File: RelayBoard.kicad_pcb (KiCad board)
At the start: 4 copper layers, 211.1 x 95.2 mm, 103 parts, among them J1 CONN_03-SCREW-5MM, J10 AC In, J11 CONN_03-SCREW-5MM, J12 CONN_03-SCREW-5MM, J13 CONN_03-SCREW-5MM, J14 CONN_03-SCREW-5MM, J15 CONN_03-SCREW-5MM, J16 CONN_03-SCREW-5MM, J17 CONN_03-SCREW-5MM, J18 CONN_03-SCREW-5MM, J19 Raspberry_Pi_2_3, J2 CONN_03-SCREW-5MM, J22 Conn_01x04, J3 CONN_03-SCREW-5MM, J4 CONN_03-SCREW-5MM, J5 CONN_03-SCREW-5MM, J6 CONN_03-SCREW-5MM, J7 CONN_03-SCREW-5MM, J8 CONN_03-SCREW-5MM, J9 PJ-202A, Q1 ULN2803ADWR, Q2 ULN2803ADWR, U1 TLP148G, U11 TLP148G, U12 TLP148G, U13 TLP148G, U14 TLP148G, U15 TLP148G, U16 TLP148G, U17 TLP148G, U18 TLP148G, U2 TLP148G, U3 TLP148G, U4 TLP148G, U5 TLP148G, U6 TLP148G, U7 TLP148G, U8 TLP148G

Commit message: final touches
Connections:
- net Net-(PS1-Pad4) renamed DC In from AC
- J9 pad PWR: DC_IN -> (no net)
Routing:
- net GND: track 1.25 -> 0.18 mm
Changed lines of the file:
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@@
   (net 131 "unconnected-(J19-Pad37)")
   (net 132 "Net-(J19-Pad38)")
-  (net 133 "Net-(PS1-Pad4)")
-  (net 134 "DC_IN")
-  (net 135 "AC_L_In")
-  (net 136 "AC_N_In")
+  (net 133 "DC_IN")
+  (net 134 "AC_L_In")
+  (net 135 "AC_N_In")
+  (net 136 "DC In from AC")
   (footprint "Resistor_SMD:R_0402_1005Metric" (layer "F.Cu")
     (at 66.829 78.003)
@@
     (fp_arc (start -1.42 -4.13) (mid -1.718466 -4.559406) (end -1.562972 -5.058699) (layer "F.Fab") (width 0.1))
     (pad "1" thru_hole rect (at 0 0 90) (size 1.98 3.96) (drill 1.32) (layers *.Cu *.Mask)
-      (net 136 "AC_N_In") (pinfunction "Pin_1") (pintype "passive"))
+      (net 135 "AC_N_In") (pinfunction "Pin_1") (pintype "passive"))
     (pad "2" thru_hole oval (at 5 0 90) (size 1.98 3.96) (drill 1.32) (layers *.Cu *.Mask)
-      (net 135 "AC_L_In") (pinfunction "Pin_2") (pintype "passive"))
+      (net 134 "AC_L_In") (pinfunction "Pin_2") (pintype "passive"))
     (model "${KICAD6_3DMODEL_DIR}/TerminalBlock.3dshapes/TerminalBlock_Altech_AK300-2_P5.00mm.wrl"
       (offset (xyz 0 0 0))
@@
     (fp_line (start -1.27 0) (end 0 -1.27) (layer "F.Fab") (width 0.1))
     (pad "1" thru_hole rect (at 0 0) (size 1.7 1.7) (drill 1) (layers *.Cu *.Mask)
-      (net 134 "DC_IN") (pinfunction "Pin_1") (pintype "passive"))
+      (net 133 "DC_IN") (pinfunction "Pin_1") (pintype "passive"))
     (pad "2" thru_hole oval (at 2.54 0) (size 1.7 1.7) (drill 1) (layers *.Cu *.Mask)
       (net 1 "VBUS") (pinfunction "Pin_2") (pintype "passive"))
     (pad "3" thru_hole oval (at 0 2.54) (size 1.7 1.7) (drill 1) (layers *.Cu *.Mask)
-      (net 133 "Net-(PS1-Pad4)") (pinfunction "Pin_3") (pintype "passive"))
+      (net 136 "DC In from AC") (pinfunction "Pin_3") (pintype "passive"))
     (pad "4" thru_hole oval (at 2.54 2.54) (size 1.7 1.7) (drill 1) (layers *.Cu *.Mask)
       (net 1 "VBUS") (pinfunction "Pin_4") (pintype "passive"))
@@
       (solder_mask_margin 0.1016))
     (pad "PWR" thru_hole circle locked (at 0 -13.87602 270) (size 4.1148 4.1148) (drill 3.19786) (layers *.Cu *.Mask)
-      (net 134 "DC_IN") (solder_mask_margin 0.1016))
+      (solder_mask_margin 0.1016))
   )
   (footprint "Resistor_SMD:R_0402_1005Metric" (layer "F.Cu")
@@
     (fp_line (start 1 -3.5) (end 0 -2.5) (layer "F.Fab") (width 0.1))
     (pad "1" thru_hole rect (at 0 0 180) (size 2.3 2) (drill 0.8) (layers *.Cu *.Mask)
-      (net 136 "AC_N_In") (pinfunction "AC/N") (pintype "power_in"))
+      (net 135 "AC_N_In") (pinfunction "AC/N") (pintype "power_in"))
     (pad "2" thru_hole circle (at 0 15.2 180) (size 2.3 2.3) (drill 0.8) (layers *.Cu *.Mask)
-      (net 135 "AC_L_In") (pinfunction "AC/L") (pintype "power_in"))
+      (net 134 "AC_L_In") (pinfunction "AC/L") (pintype "power_in"))
     (pad "3" thru_hole circle (at 28 0 180) (size 2.3 2.3) (drill 0.76) (layers *.Cu *.Mask)
       (net 2 "GND") (pinfunction "-Vo") (pintype "power_out"))
     (pad "4" thru_hole circle (at 28 7.6 180) (size 2.3 2.3) (drill 0.76) (layers *.Cu *.Mask)
-      (net 133 "Net-(PS1-Pad4)") (pinfunction "+Vo") (pintype "power_out"))
+      (net 136 "DC In from AC") (pinfunction "+Vo") (pintype "power_out"))
     (model "${KICAD6_3DMODEL_DIR}/Converter_ACDC.3dshapes/Converter_ACDC_MeanWell_IRM-02-xx_THT.wrl"
       (offset (xyz 0 0 0))
@@
   (segment (start 138.32587 86.89) (end 138.32629 86.88958) (width 0.25) (layer "F.Cu") (net 2))
   (segment (start 155.90001 87.495) (end 156.075 87.495) (width 0.25) (layer "F.Cu") (net 2))
-  (segment (start 66.985 69.405) (end 66.985 70.465774) (width 0.25) (layer "F.Cu") (net 2))
   (segment (start 208.23958 87.83) (end 208.245 87.83542) (width 0.25) (layer "F.Cu") (net 2))
-  (segment (start 66.985 70.465774) (end 66.985857 70.466631) (width 0.25) (layer "F.Cu") (net 2))
   (via (at 123.976119 140.073969) (size 0.6) (drill 0.3) (layers "F.Cu" "B.Cu") (free) (net 2))
   (via (at 107.696 120.65) (size 0.8) (drill 0.4) (layers "F.Cu" "B.Cu") (net 2))
-  (via (at 66.985857 70.466631) (size 0.8) (drill 0.4) (layers "F.Cu" "B.Cu") (free) (net 2))
+  (via (at 66.912776 69.432558) (size 0.8) (drill 0.4) (layers "F.Cu" "B.Cu") (free) (net 2))
   (via (at 23.82653 110.2401) (size 3.5) (drill 2.75) (layers "F.Cu" "B.Cu") (free) (net 2))
   (via (at 155.901949 140.740284) (size 0.6) (drill 0.3) (layers "F.Cu" "B.Cu") (free) (net 2))
@@
   (segment (start 107.57 111.83) (end 97.098 111.83) (width 0.25) (layer "F.Cu") (net 132))
   (segment (start 97.028 111.76) (end 94.54648 114.24152) (width 0.25) (layer "F.Cu") (net 132))
-  (segment (start 20.32 88.392) (end 20.32 92.456) (width 1) (layer "B.Cu") (net 133))
-  (segment (start 27.94 100.076) (end 49.784 100.076) (width 1) (layer "B.Cu") (net 133))
-  (segment (start 163.555832 112.728332) (end 173.026419 112.728332) (width 1) (layer "B.Cu") (net 133))
-  (segment (start 50.038 99.822) (end 64.008 99.822) (width 1) (layer "B.Cu") (net 133))
-  (segment (start 66.972489 102.786489) (end 70.274489 102.786489) (width 1) (layer "B.Cu") (net 133))
-  (segment (start 21.59 87.122) (end 20.32 88.392) (width 1) (layer "B.Cu") (net 133))
-  (segment (start 64.008 99.822) (end 66.972489 102.786489) (width 1) (layer "B.Cu") (net 133))
-  (segment (start 70.728 103.24) (end 154.0675 103.24) (width 1) (layer "B.Cu") (net 133))
-  (segment (start 154.0675 103.24) (end 163.555832 112.728332) (width 1) (layer "B.Cu") (net 133))
-  (segment (start 20.32 92.456) (end 27.94 100.076) (width 1) (layer "B.Cu") (net 133))
-  (segment (start 70.274489 102.786489) (end 70.728 103.24) (width 1) (layer "B.Cu") (net 133))
-  (segment (start 49.784 100.076) (end 50.038 99.822) (width 1) (layer "B.Cu") (net 133))
-  (segment (start 26.924 69.85) (end 48.26 69.85) (width 1) (layer "F.Cu") (net 134))
-  (segment (start 49.784 73.406) (end 47.92853 75.26147) (width 1) (layer "F.Cu") (net 134))
-  (segment (start 49.784 71.374) (end 49.784 73.406) (width 1) (layer "F.Cu") (net 134))
-  (segment (start 47.92853 75.26147) (end 44.89631 75.26147) (width 1) (layer "F.Cu") (net 134))
-  (segment (start 21.59 84.582) (end 21.59 75.184) (width 1) (layer "F.Cu") (net 134))
-  (segment (start 21.59 75.184) (end 26.924 69.85) (width 1) (layer "F.Cu") (net 134))
-  (segment (start 48.26 69.85) (end 49.784 71.374) (width 1) (layer "F.Cu") (net 134))
-  (segment (start 217.650332 105.128332) (end 220.726 108.204) (width 1) (layer "F.Cu") (net 135))
-  (segment (start 206.988919 105.128332) (end 217.650332 105.128332) (width 1) (layer "F.Cu") (net 135))
-  (segment (start 206.988919 105.128332) (end 201.026419 105.128332) (width 1) (layer "F.Cu") (net 135))
-  (segment (start 220.726 108.204) (end 220.726 109.554) (width 1) (layer "F.Cu") (net 135))
-  (segment (start 201.026419 120.328332) (end 215.967668 120.328332) (width 1) (layer "F.Cu") (net 136))
-  (segment (start 220.726 115.57) (end 220.726 114.554) (width 1) (layer "F.Cu") (net 136))
-  (segment (start 215.967668 120.328332) (end 220.726 115.57) (width 1) (layer "F.Cu") (net 136))
+  (segment (start 26.924 69.85) (end 48.26 69.85) (width 1) (layer "F.Cu") (net 133))
+  (segment (start 49.784 73.406) (end 47.92853 75.26147) (width 1) (layer "F.Cu") (net 133))
+  (segment (start 49.784 71.374) (end 49.784 73.406) (width 1) (layer "F.Cu") (net 133))
+  (segment (start 47.92853 75.26147) (end 44.89631 75.26147) (width 1) (layer "F.Cu") (net 133))
+  (segment (start 21.59 84.582) (end 21.59 75.184) (width 1) (layer "F.Cu") (net 133))
+  (segment (start 21.59 75.184) (end 26.924 69.85) (width 1) (layer "F.Cu") (net 133))
+  (segment (start 48.26 69.85) (end 49.784 71.374) (width 1) (layer "F.Cu") (net 133))
+  (segment (start 217.650332 105.128332) (end 220.726 108.204) (width 1) (layer "F.Cu") (net 134))
+  (segment (start 206.988919 105.128332) (end 217.650332 105.128332) (width 1) (layer "F.Cu") (net 134))
+  (segment (start 206.988919 105.128332) (end 201.026419 105.128332) (width 1) (layer "F.Cu") (net 134))
+  (segment (start 220.726 108.204) (end 220.726 109.554) (width 1) (layer "F.Cu") (net 134))
+  (segment (start 201.026419 120.328332) (end 215.967668 120.328332) (width 1) (layer "F.Cu") (net 135))
+  (segment (start 220.726 115.57) (end 220.726 114.554) (width 1) (layer "F.Cu") (net 135))
+  (segment (start 215.967668 120.328332) (end 220.726 115.57) (width 1) (layer "F.Cu") (net 135))
+  (segment (start 20.32 88.392) (end 20.32 92.456) (width 1) (layer "B.Cu") (net 136))
+  (segment (start 27.94 100.076) (end 49.784 100.076) (width 1) (layer "B.Cu") (net 136))
+  (segment (start 163.555832 112.728332) (end 173.026419 112.728332) (width 1) (layer "B.Cu") (net 136))
+  (segment (start 50.038 99.822) (end 64.008 99.822) (width 1) (layer "B.Cu") (net 136))
+  (segment (start 66.972489 102.786489) (end 70.274489 102.786489) (width 1) (layer "B.Cu") (net 136))
+  (segment (start 21.59 87.122) (end 20.32 88.392) (width 1) (layer "B.Cu") (net 136))
+  (segment (start 64.008 99.822) (end 66.972489 102.786489) (width 1) (layer "B.Cu") (net 136))
+  (segment (start 70.728 103.24) (end 154.0675 103.24) (width 1) (layer "B.Cu") (net 136))
+  (segment (start 154.0675 103.24) (end 163.555832 112.728332) (width 1) (layer "B.Cu") (net 136))
+  (segment (start 20.32 92.456) (end 27.94 100.076) (width 1) (layer "B.Cu") (net 136))
+  (segment (start 70.274489 102.786489) (end 70.728 103.24) (width 1) (layer "B.Cu") (net 136))
+  (segment (start 49.784 100.076) (end 50.038 99.822) (width 1) (layer "B.Cu") (net 136))
   (zone (net 2) (net_name "GND") (layer "F.Cu") (hatch edge 0.508)
     (connect_pads (clearance 0.508))

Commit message: drc run after connector fix
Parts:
- J19: moved to F.Cu
- moved J19 2.55 mm to (28.7, 111.5), turned to 90 degrees
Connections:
- J9 pad PWR: (no net) -> DC_IN
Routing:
- net VBUS: track 87.0 -> 68.3 mm
- net Net-(Q2-Pad7): track 78.1 -> 94.1 mm, vias 1 -> 2
- net Net-(Q2-Pad8): track 76.1 -> 88.3 mm, vias 1 -> 3
- net Net-(Q2-Pad1): track 75.3 -> 84.2 mm
- net DC In from AC: track 167.2 -> 175.5 mm
- net Net-(Q2-Pad2): track 73.0 -> 80.0 mm
- net Net-(J19-Pad12): track 71.1 -> 77.7 mm
- net Net-(J19-Pad38): track 36.9 -> 43.3 mm, vias 0 -> 2
- net Net-(J19-Pad11): track 74.8 -> 68.7 mm, vias 0 -> 2
- net Net-(Q1-Pad1): track 34.3 -> 38.0 mm, vias 0 -> 2
- net Net-(Q2-Pad4): track 93.0 -> 96.6 mm, vias 2 -> 1
- net Net-(Q2-Pad3): track 90.4 -> 87.0 mm, vias 1 -> 2
- net Net-(Q2-Pad6): track 98.9 -> 101.8 mm, vias 2 -> 3
- net I2C_SCL: track 56.1 -> 58.8 mm
- net Net-(J19-Pad8): track 76.6 -> 79.2 mm
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
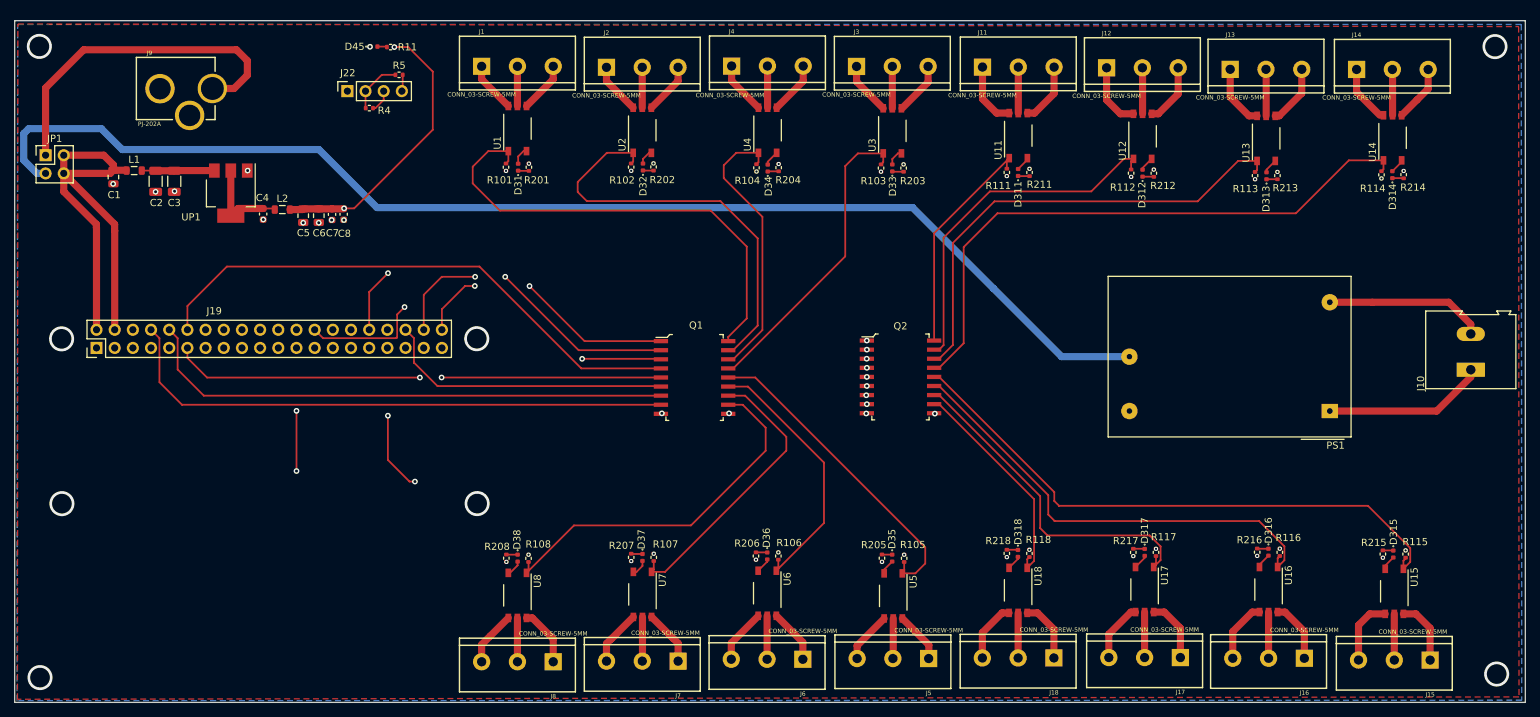
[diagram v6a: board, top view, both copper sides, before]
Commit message: total rewrite, solid state relays & change all footprints to 0805s
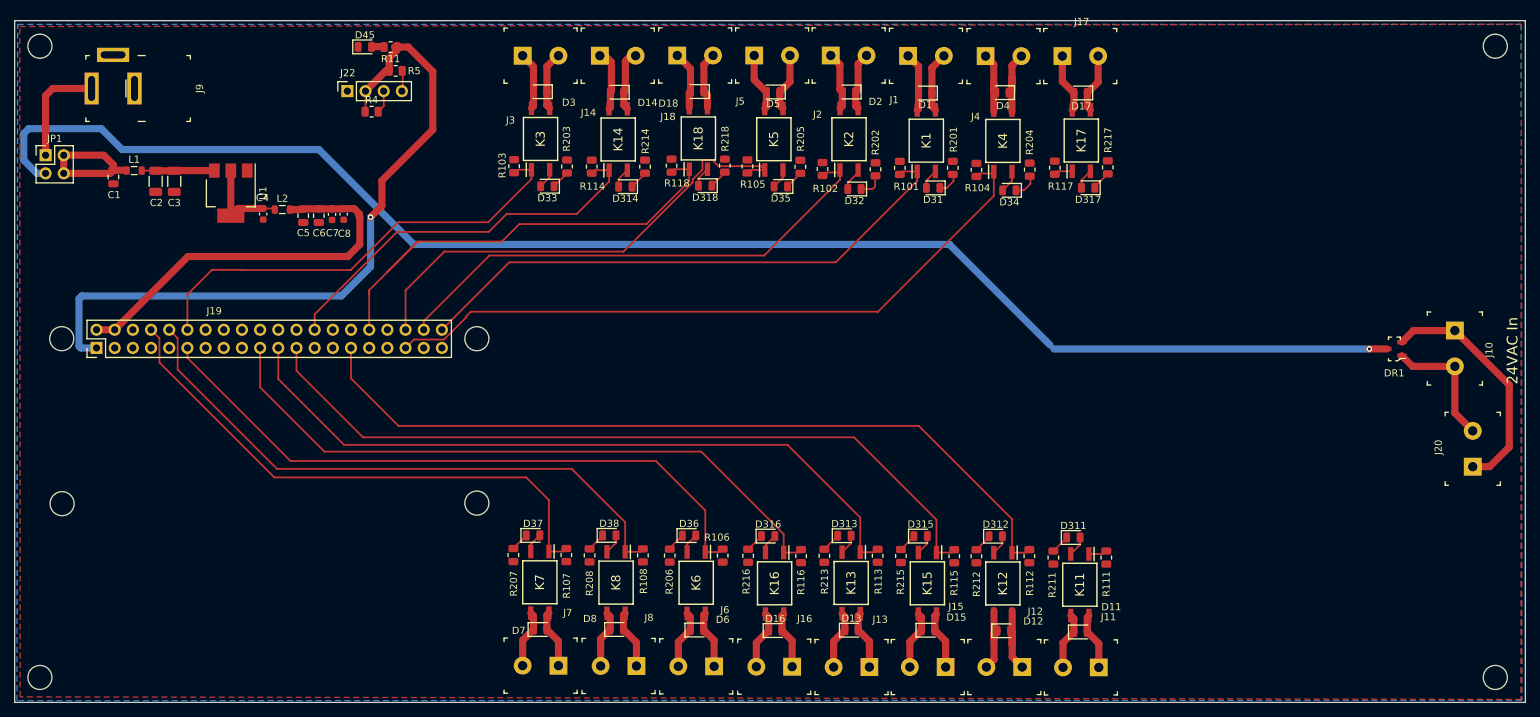
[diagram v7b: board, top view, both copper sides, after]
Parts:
- removed PS1: IRM-02-5, Converter_ACDC:Converter_ACDC_MeanWell_IRM-02-xx_THT
- removed Q1, Q2: ULN2803ADWR, digikey-footprints:SOIC-18_W7.5mm
- removed U11, U12, U13, U14, U15, U16, U17, U18, U2, U3, U4, U5, U6, U7, U8: TLP148G, Package_SO:MFSOP6-5_4.4x3.6mm_P1.27mm
- removed UP1: AP1117-33, Package_TO_SOT_SMD:SOT-223-3_TabPin2
- added D1: D, Diode_SMD:D_0805_2012Metric, F.Cu at (144.5, 75.9)
- added D11: D, Diode_SMD:D_0805_2012Metric, F.Cu at (166.2, 151.2)
- added D12: D, Diode_SMD:D_0805_2012Metric, F.Cu at (155.5, 151.0)
- added D13: D, Diode_SMD:D_0805_2012Metric, F.Cu at (134.2, 150.9)
- added D14: D, Diode_SMD:D_0805_2012Metric, F.Cu at (101.5, 75.8)
- added D15: D, Diode_SMD:D_0805_2012Metric, F.Cu at (144.9, 150.9)
- added D16: D, Diode_SMD:D_0805_2012Metric, F.Cu at (123.5, 151.0)
- added D17: D, Diode_SMD:D_0805_2012Metric, F.Cu at (166.2, 75.9)
- added D18: D, Diode_SMD:D_0805_2012Metric, F.Cu at (112.6, 75.7)
- added D2: D, Diode_SMD:D_0805_2012Metric, F.Cu at (133.8, 75.8)
- added D3: D, Diode_SMD:D_0805_2012Metric, F.Cu at (90.7, 75.7)
- added D4: D, Diode_SMD:D_0805_2012Metric, F.Cu at (155.3, 75.8)
- added D5: D, Diode_SMD:D_0805_2012Metric, F.Cu at (123.2, 75.8)
- added D6: D, Diode_SMD:D_0805_2012Metric, F.Cu at (112.6, 150.9)
- added D7: D, Diode_SMD:D_0805_2012Metric, F.Cu at (90.7, 150.9)
- added D8: D, Diode_SMD:D_0805_2012Metric, F.Cu at (101.4, 150.8)
- added DR1: BAT54SLT1G, digikey-footprints:SOT-23-3, F.Cu at (210.1, 111.7)
- added J20: OSTTC020162, digikey-footprints:Term_Block_1x2_P5mm, F.Cu at (221.0, 128.1)
- added K1: AQY212GHAX, Panasonic-SSR:SOP254P962X315-4N, F.Cu at (144.7, 82.5)
- added K11: AQY212GHAX, Panasonic-SSR:SOP254P962X315-4N, F.Cu at (166.1, 144.6)
- added K12: AQY212GHAX, Panasonic-SSR:SOP254P962X315-4N, F.Cu at (155.3, 144.4)
- added K13: AQY212GHAX, Panasonic-SSR:SOP254P962X315-4N, F.Cu at (134.2, 144.3)
- added K14: AQY212GHAX, Panasonic-SSR:SOP254P962X315-4N, F.Cu at (101.6, 82.4)
- added K15: AQY212GHAX, Panasonic-SSR:SOP254P962X315-4N, F.Cu at (144.8, 144.4)
- added K16: AQY212GHAX, Panasonic-SSR:SOP254P962X315-4N, F.Cu at (123.5, 144.4)
- added K17: AQY212GHAX, Panasonic-SSR:SOP254P962X315-4N, F.Cu at (166.3, 82.5)
- added K18: AQY212GHAX, Panasonic-SSR:SOP254P962X315-4N, F.Cu at (112.8, 82.2)
- added K2: AQY212GHAX, Panasonic-SSR:SOP254P962X315-4N, F.Cu at (133.8, 82.3)
- added K3: AQY212GHAX, Panasonic-SSR:SOP254P962X315-4N, F.Cu at (90.8, 82.3)
- added K4: AQY212GHAX, Panasonic-SSR:SOP254P962X315-4N, F.Cu at (155.3, 82.6)
- added K5: AQY212GHAX, Panasonic-SSR:SOP254P962X315-4N, F.Cu at (123.3, 82.3)
- added K6: AQY212GHAX, Panasonic-SSR:SOP254P962X315-4N, F.Cu at (112.5, 144.3)
- added K7: AQY212GHAX, Panasonic-SSR:SOP254P962X315-4N, F.Cu at (90.7, 144.3)
- added K8: AQY212GHAX, Panasonic-SSR:SOP254P962X315-4N, F.Cu at (101.3, 144.3)
- D31, D32, D33, D34, D45: footprint LED_SMD:LED_0402_1005Metric -> LED_SMD:LED_0805_2012Metric
- D311: renamed from D312; footprint LED_SMD:LED_0402_1005Metric -> LED_SMD:LED_0805_2012Metric
- D312: renamed from D311; footprint LED_SMD:LED_0402_1005Metric -> LED_SMD:LED_0805_2012Metric
- D313: renamed from D314; footprint LED_SMD:LED_0402_1005Metric -> LED_SMD:LED_0805_2012Metric
- D314: renamed from D313; footprint LED_SMD:LED_0402_1005Metric -> LED_SMD:LED_0805_2012Metric
- D315: renamed from D316; footprint LED_SMD:LED_0402_1005Metric -> LED_SMD:LED_0805_2012Metric
- D316: renamed from D315; footprint LED_SMD:LED_0402_1005Metric -> LED_SMD:LED_0805_2012Metric
- D317: renamed from D318; footprint LED_SMD:LED_0402_1005Metric -> LED_SMD:LED_0805_2012Metric
- D318: renamed from D317; footprint LED_SMD:LED_0402_1005Metric -> LED_SMD:LED_0805_2012Metric
- D35: renamed from D36; footprint LED_SMD:LED_0402_1005Metric -> LED_SMD:LED_0805_2012Metric
- D36: renamed from D35; footprint LED_SMD:LED_0402_1005Metric -> LED_SMD:LED_0805_2012Metric
- D37: renamed from D38; footprint LED_SMD:LED_0402_1005Metric -> LED_SMD:LED_0805_2012Metric
- D38: renamed from D37; footprint LED_SMD:LED_0402_1005Metric -> LED_SMD:LED_0805_2012Metric
- J1, J11, J12, J13, J14, J15, J16, J17, J18, J2, J3, J4, J5, J6, J7, J8: value CONN_03-SCREW-5MM -> OSTTC020162; footprint Connectors:SCREWTERMINAL-5MM-3 -> digikey-footprints:Term_Block_1x2_P5mm
- J10: value AC In -> 24VAC In; footprint TerminalBlock:TerminalBlock_Altech_AK300-2_P5.00mm -> digikey-footprints:Term_Block_1x2_P5mm
- J9: footprint Connectors:POWER_JACK_PTH_LOCK -> digikey-footprints:Barrel_Jack_5.5mmODx2.1mmID_PJ-202A
- R101, R102, R103, R104, R11, R201, R202, R203, R204, R4, R5: footprint Resistor_SMD:R_0402_1005Metric -> Resistor_SMD:R_0805_2012Metric
- R105: renamed from R106; footprint Resistor_SMD:R_0402_1005Metric -> Resistor_SMD:R_0805_2012Metric
- R106: renamed from R105; footprint Resistor_SMD:R_0402_1005Metric -> Resistor_SMD:R_0805_2012Metric
- R107: renamed from R108; footprint Resistor_SMD:R_0402_1005Metric -> Resistor_SMD:R_0805_2012Metric
- R108: renamed from R107; footprint Resistor_SMD:R_0402_1005Metric -> Resistor_SMD:R_0805_2012Metric
- R111: renamed from R112; footprint Resistor_SMD:R_0402_1005Metric -> Resistor_SMD:R_0805_2012Metric
- R112: renamed from R111; footprint Resistor_SMD:R_0402_1005Metric -> Resistor_SMD:R_0805_2012Metric
- R113: renamed from R114; footprint Resistor_SMD:R_0402_1005Metric -> Resistor_SMD:R_0805_2012Metric
- R114: renamed from R113; footprint Resistor_SMD:R_0402_1005Metric -> Resistor_SMD:R_0805_2012Metric
- R115: renamed from R116; footprint Resistor_SMD:R_0402_1005Metric -> Resistor_SMD:R_0805_2012Metric
- R116: renamed from R115; footprint Resistor_SMD:R_0402_1005Metric -> Resistor_SMD:R_0805_2012Metric
- R117: renamed from R118; footprint Resistor_SMD:R_0402_1005Metric -> Resistor_SMD:R_0805_2012Metric
- R118: renamed from R117; footprint Resistor_SMD:R_0402_1005Metric -> Resistor_SMD:R_0805_2012Metric
- R205: renamed from R206; footprint Resistor_SMD:R_0402_1005Metric -> Resistor_SMD:R_0805_2012Metric
- R206: renamed from R205; footprint Resistor_SMD:R_0402_1005Metric -> Resistor_SMD:R_0805_2012Metric
- R207: renamed from R208; footprint Resistor_SMD:R_0402_1005Metric -> Resistor_SMD:R_0805_2012Metric
- R208: renamed from R207; footprint Resistor_SMD:R_0402_1005Metric -> Resistor_SMD:R_0805_2012Metric
- R211: renamed from R212; footprint Resistor_SMD:R_0402_1005Metric -> Resistor_SMD:R_0805_2012Metric
- R212: renamed from R211; footprint Resistor_SMD:R_0402_1005Metric -> Resistor_SMD:R_0805_2012Metric
- R213: renamed from R214; footprint Resistor_SMD:R_0402_1005Metric -> Resistor_SMD:R_0805_2012Metric
- R214: renamed from R213; footprint Resistor_SMD:R_0402_1005Metric -> Resistor_SMD:R_0805_2012Metric
- R215: renamed from R216; footprint Resistor_SMD:R_0402_1005Metric -> Resistor_SMD:R_0805_2012Metric
- R216: renamed from R215; footprint Resistor_SMD:R_0402_1005Metric -> Resistor_SMD:R_0805_2012Metric
- R217: renamed from R218; footprint Resistor_SMD:R_0402_1005Metric -> Resistor_SMD:R_0805_2012Metric
- R218: renamed from R217; footprint Resistor_SMD:R_0402_1005Metric -> Resistor_SMD:R_0805_2012Metric
- U1: value TLP148G -> AP1117-50; footprint Package_SO:MFSOP6-5_4.4x3.6mm_P1.27mm -> Package_TO_SOT_SMD:SOT-223-3_TabPin2
- moved J14 105.8 mm to (99.0, 70.7)
- moved J18 99.3 mm to (109.8, 70.7), turned to 0 degrees
- moved J13 97.6 mm to (136.7, 156.1), turned to 180 degrees
- moved R213 96.9 mm to (130.4, 140.6), turned to 90 degrees
- moved R114 92.7 mm to (97.9, 86.2), turned to 90 degrees
- moved D313 91.7 mm to (133.2, 137.8), turned to 0 degrees
- moved D314 89.6 mm to (102.6, 89.0), turned to 180 degrees
- moved R216 88.7 mm to (119.8, 140.6)
- moved R214 88.4 mm to (105.3, 86.2)
- moved R113 88.3 mm to (137.8, 140.6)
- moved J5 87.7 mm to (120.6, 70.7), turned to 0 degrees
- moved D316 87.4 mm to (122.5, 137.8), turned to 0 degrees
- moved R118 86.6 mm to (109.1, 86.0)
- moved J17 85.6 mm to (163.7, 70.7), turned to 0 degrees
- moved J11 85.4 mm to (168.8, 156.2), turned to 180 degrees
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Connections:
- C4 pad 1: Net-(C4-Pad1) -> 5V
- C5 pad 1: MCU_VCC -> Net-(C5-Pad1)
- C6 pad 1: MCU_VCC -> Net-(C5-Pad1)
- C7 pad 1: MCU_VCC -> Net-(C5-Pad1)
- C8 pad 1: MCU_VCC -> Net-(C5-Pad1)
- J1 pad 1: Net-(J1-Pad1) -> Net-(D1-Pad2)
- J1 pad 2: Net-(J1-Pad2) -> Net-(D1-Pad1)
- J19 pad 1: unconnected-(J19-Pad1) -> +3V3
- J19 pad 17: unconnected-(J19-Pad17) -> +3V3
- J19 pad 19: Net-(Q2-Pad5) -> Net-(J19-Pad19)
- J19 pad 2: VBUS -> 5V
- J19 pad 21: Net-(Q2-Pad4) -> Net-(J19-Pad21)
- J19 pad 23: Net-(Q2-Pad6) -> Net-(J19-Pad23)
- J19 pad 26: Net-(Q2-Pad3) -> Net-(J19-Pad26)
- J19 pad 29: Net-(Q2-Pad1) -> Net-(J19-Pad29)
- J19 pad 31: Net-(Q2-Pad2) -> Net-(J19-Pad31)
- J19 pad 32: Net-(Q2-Pad7) -> Net-(J19-Pad32)
- J19 pad 33: Net-(Q2-Pad8) -> Net-(J19-Pad33)
- J19 pad 4: VBUS -> 5V
- J19 pad 40: Net-(Q1-Pad1) -> Net-(J19-Pad40)
- J22 pad 2: MCU_VCC -> +3V3
- JP1 pad 3: DC In from AC -> 16VDC Unregulated In from AC
- L2 pad 1: Net-(C4-Pad1) -> 5V
- L2 pad 2: MCU_VCC -> Net-(C5-Pad1)
- R101 pad 1: Net-(Q1-Pad18) -> Net-(J19-Pad40)
- R102 pad 1: Net-(Q1-Pad17) -> Net-(J19-Pad38)
- R103 pad 1: Net-(Q1-Pad15) -> Net-(J19-Pad12)
- R104 pad 1: Net-(Q1-Pad16) -> Net-(J19-Pad35)
- R105 pad 1: Net-(Q1-Pad13) -> Net-(J19-Pad36)
- R106 pad 1: Net-(Q1-Pad14) -> Net-(J19-Pad11)
- R107 pad 1: Net-(Q1-Pad11) -> Net-(J19-Pad8)
- R108 pad 1: Net-(Q1-Pad12) -> Net-(J19-Pad10)
- R11 pad 1: MCU_VCC -> +3V3
- R111 pad 1: Net-(Q2-Pad17) -> Net-(J19-Pad31)
- R112 pad 1: Net-(Q2-Pad18) -> Net-(J19-Pad29)
- R113 pad 1: Net-(Q2-Pad15) -> Net-(J19-Pad21)
- R114 pad 1: Net-(Q2-Pad16) -> Net-(J19-Pad26)
- R115 pad 1: Net-(Q2-Pad13) -> Net-(J19-Pad23)
- R116 pad 1: Net-(Q2-Pad14) -> Net-(J19-Pad19)
- R117 pad 1: Net-(Q2-Pad11) -> Net-(J19-Pad33)
- R118 pad 1: Net-(Q2-Pad12) -> Net-(J19-Pad32)
- R4 pad 1: MCU_VCC -> +3V3
- R5 pad 1: MCU_VCC -> +3V3
- U1 pad 1: Net-(Q1-Pad18) -> GND
- U1 pad 3: Net-(D31-Pad2) -> Net-(C2-Pad1)
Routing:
- net 16VDC Unregulated In from AC: track 0.00 -> 210.3 mm, vias 0 -> 1
- net DC In from AC: track 175.5 -> 0.00 mm
- net Net-(J19-Pad29): track 0.00 -> 112.1 mm
- net Net-(J19-Pad23): track 0.00 -> 108.9 mm
- net Net-(Q2-Pad6): track 101.8 -> 0.00 mm, vias 3 -> 0
- net Net-(Q2-Pad5): track 101.3 -> 0.00 mm, vias 1 -> 0
- net Net-(J19-Pad21): track 0.00 -> 101.1 mm
- net +3V3: track 0.00 -> 100.0 mm, vias 0 -> 1
- net Net-(Q2-Pad4): track 96.6 -> 0.00 mm, vias 1 -> 0
- net Net-(Q2-Pad7): track 94.1 -> 0.00 mm, vias 2 -> 0
- net Net-(J19-Pad19): track 0.00 -> 92.3 mm
- net Net-(Q2-Pad8): track 88.3 -> 0.00 mm, vias 3 -> 0
- net Net-(Q2-Pad3): track 87.0 -> 0.00 mm, vias 2 -> 0
- net Net-(Q2-Pad15): track 84.3 -> 0.00 mm
- net Net-(Q2-Pad1): track 84.2 -> 0.00 mm, vias 1 -> 0
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- added copper zone on B.Cu, net Net-(C5-Pad1)
- removed copper zone on B.Cu, net MCU_VCC
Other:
- outline, holes or cut-outs redrawn
- board text added: "24VAC In"
